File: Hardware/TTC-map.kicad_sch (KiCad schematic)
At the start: 35 parts, among them J1 USB_C_Receptacle_USB2.0_16P, Q1 PMOS, Q2 PMOS, Q3 PMOS, Q4 PMOS, Q5 PMOS, Q7 PMOS, U1 ESP32-DEVKIT-V1, U2 74HC595, U3 74HC595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

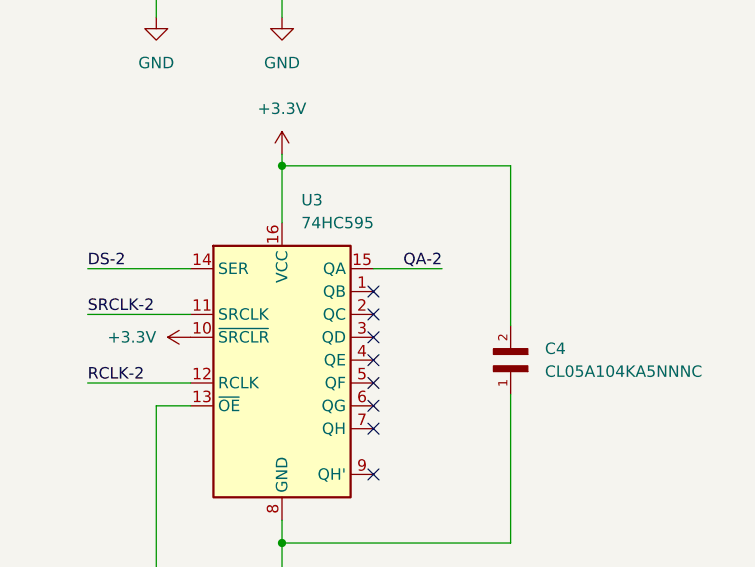
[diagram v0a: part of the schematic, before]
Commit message: Rerouted the PCB
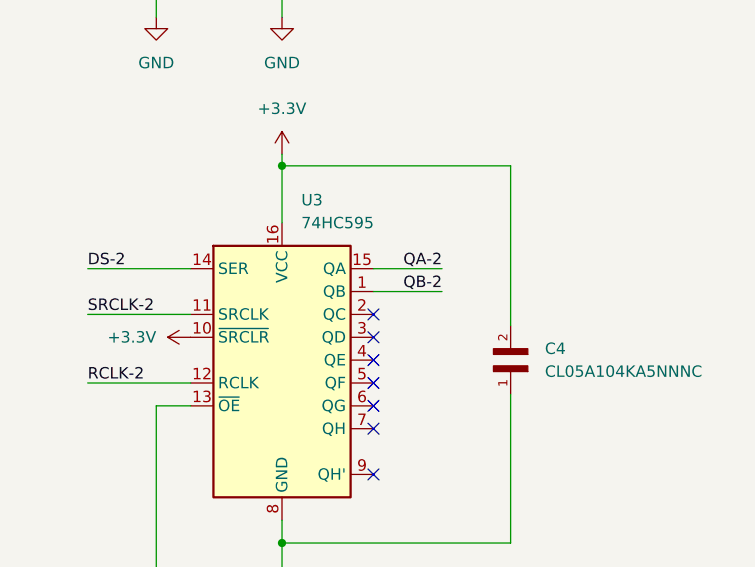
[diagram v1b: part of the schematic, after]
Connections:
- net QB-2: now also U3.1 (QB)
- no-connect marks 34 -> 33
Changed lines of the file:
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@@
-	)
-	(no_connect
-		(at 243.84 100.33)
 	)
 	(no_connect
@@
 	(wire
 		(pts
+			(xy 243.84 100.33) (xy 251.46 100.33)
+		)
+		(stroke
+			(width 0)
+			(type default)
+		)
+	)
+	(wire
+		(pts
 			(xy 259.08 86.36) (xy 259.08 104.14)
 		)
@@
 		(effects
 			(font
+				(size 1.27 1.27)
+			)
+			(justify right bottom)
+		)
+	)
+	(label "QB-2"
+		(at 251.46 100.33 180)
+		(effects
+			(font
